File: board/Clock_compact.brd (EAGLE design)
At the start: 50 x 50 mm, 18 parts

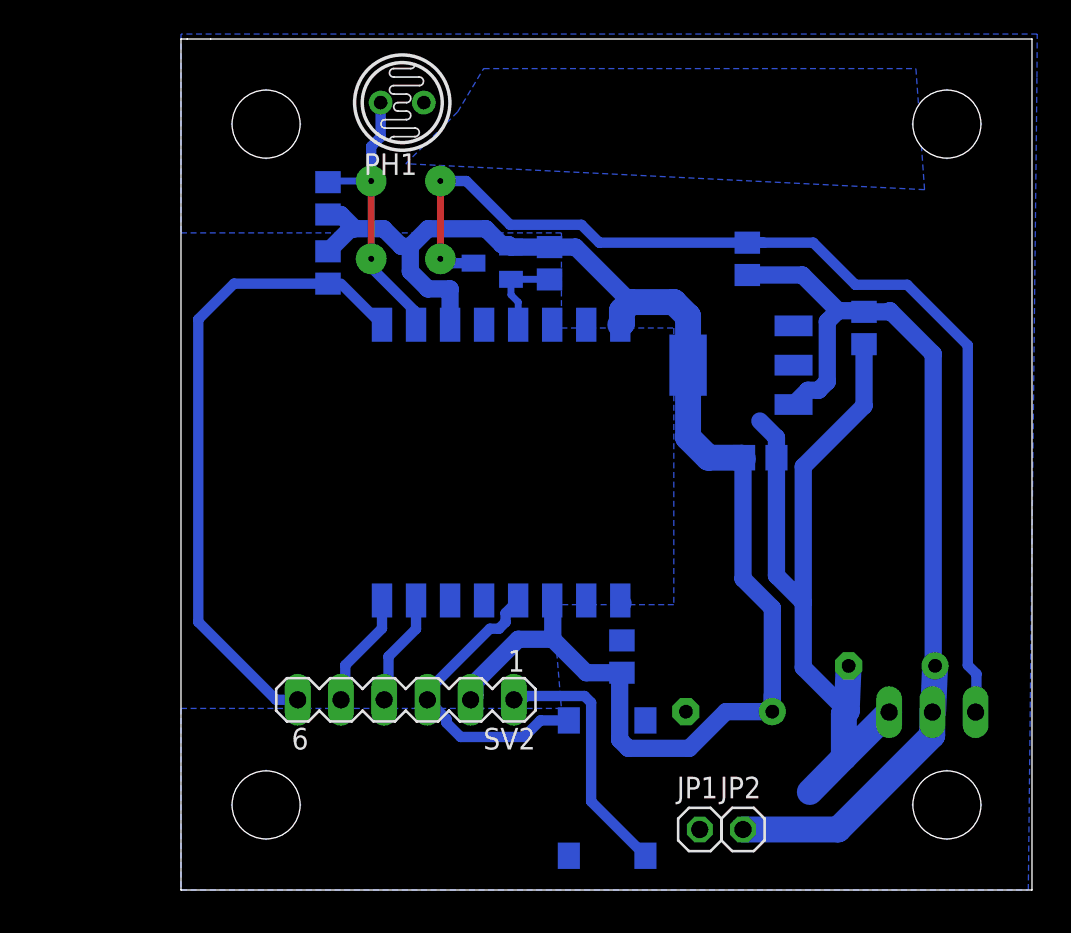
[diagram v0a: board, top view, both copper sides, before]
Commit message: Removed LEDs, organised PCB files
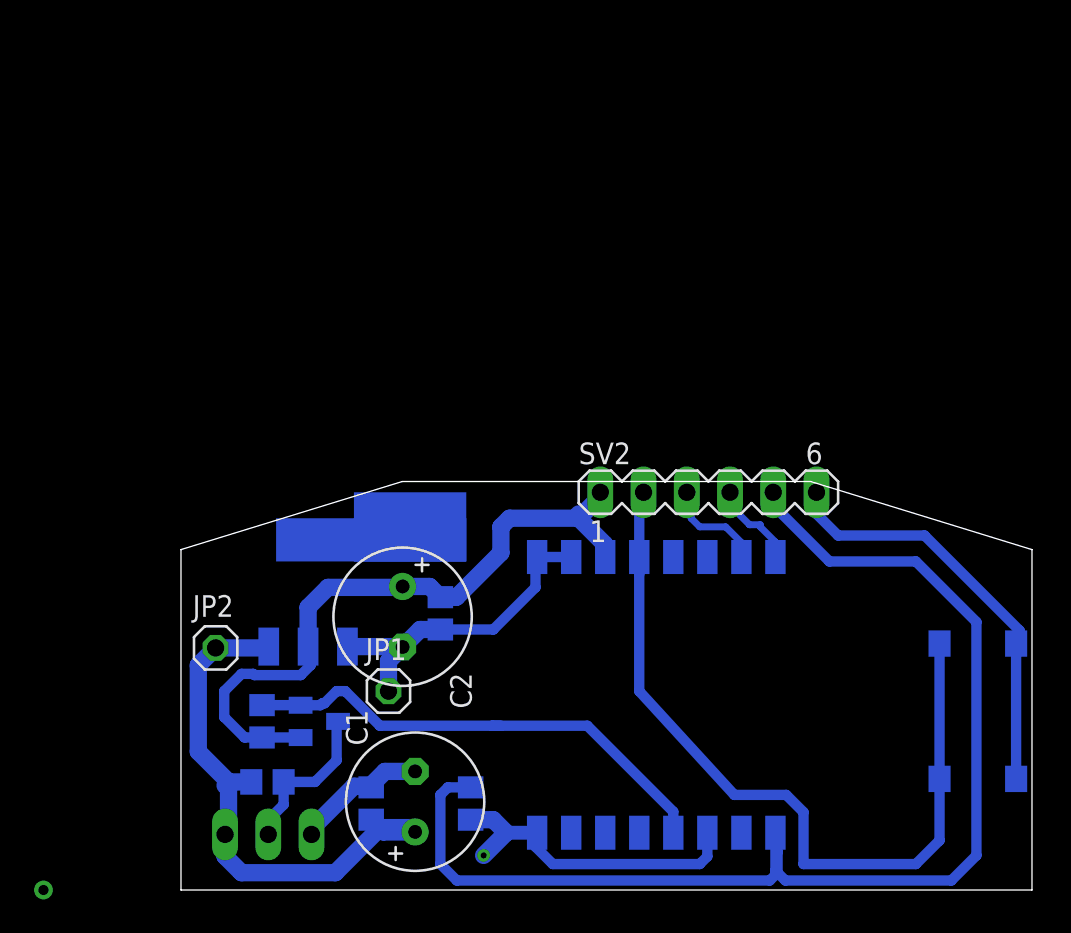
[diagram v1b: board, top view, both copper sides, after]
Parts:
- removed C5: 10nF, rcl:C0805
- removed PH1: VT20N1, photo-elements:TO46-VT200
- removed R4: (no value), rcl:R0805
- added U$3: PIN1, untitled:PIN1
- C1: value 1000uF -> (none); device rcl:TT5D11L -> rcl:E3,5-8
- C2: value 100uF -> (none); device rcl:TT5D7L -> rcl:E3,5-8
- C3, C4: value 10nF -> (none)
- R1, R2, R3: value 10k -> (none)
- SV1: value LED strip -> (none)
- SV2: value Programmer -> (none)
- moved R2 41.7 mm to (5.08, 6.35), turned to 0 degrees
- moved C3 40.2 mm to (11.2, 5.08), turned to 90 degrees
- moved SV1 39.7 mm to (5.13, 3.27), turned to 0 degrees
- moved JP2 32.8 mm to (2.03, 14.2)
- moved R3 32.6 mm to (17.0, 5.08), turned to 270 degrees
- moved R1 31.8 mm to (4.76, 9.91), turned to 270 degrees
- moved U$1 31.1 mm to (18.9, 3.36), turned to 90 degrees
- moved C1 29.1 mm to (13.8, 5.19), flipped to the top, turned to 90 degrees
- moved U$2 28.8 mm to (8.13, 9.91), turned to 90 degrees
- moved AMS1117 28.8 mm to (7.47, 17.4), turned to 0 degrees
- moved S1 22.2 mm to (46.8, 10.5)
- moved SV2 21.6 mm to (31.0, 23.4), turned to 0 degrees
- moved C4 20.9 mm to (15.2, 16.3), turned to 270 degrees
- moved JP1 20.0 mm to (12.2, 11.7)
- moved C2 20.0 mm to (13.0, 16.1), flipped to the top, turned to 270 degrees
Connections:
- removed net ADC: PH1.1, R4.1, U$1.10
- removed net GPIO14: R1.1, U$1.13, U$2.S
- new net N$9: R1.1, U$1.12, U$2.S
- net +5V: now also SV1.3; no longer SV1.2
- net GND: now also SV2.6; no longer C5.2, PH1.2, SV2.1
- net N$7: now also SV1.2; no longer SV1.3
- net PRG_EN: now also S1.2, SV2.2; no longer SV2.3
- net REST: now also SV2.5; no longer SV2.6
- net RXD: now also SV2.3; no longer SV2.4
- net TXD: now also SV2.4; no longer SV2.5
- net VCC: now also AMS1117.2, SV2.1; no longer AMS1117.TAB, C5.1, R4.2, SV2.2
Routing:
- net N$7: track 64.7 -> 9.67 mm, vias 2 -> 0
- net REST: track 42.2 -> 72.9 mm
- net PRG_EN: track 18.1 -> 48.3 mm
- net VCC: track 90.1 -> 60.5 mm, vias 0 -> 1
- net N$9: track 0.00 -> 29.2 mm
- net +5V: track 55.8 -> 33.9 mm
- net ADC: track 16.9 -> 0.00 mm, vias 2 -> 0
- net GND: track 63.2 -> 52.0 mm
- net N$5: track 8.00 -> 0.00 mm, vias 1 -> 0
- net N$4: track 8.00 -> 0.00 mm, vias 1 -> 0
- net N$2: track 8.00 -> 0.00 mm, vias 1 -> 0
- net N$1: track 8.00 -> 0.00 mm, vias 1 -> 0
- net GPIO14: track 5.11 -> 0.00 mm
- net TXD: track 6.84 -> 5.28 mm
- net RXD: track 6.61 -> 6.03 mm
- removed copper zone on layer 16, net GND
- removed copper zone on layer 16, net N$3
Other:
- board size 50 x 50 mm -> 50 x 24 mm
- board text removed: "Jakub Jendryka Jan Sobków 2017"
